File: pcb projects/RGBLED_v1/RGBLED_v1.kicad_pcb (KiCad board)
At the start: 2 copper layers, 63 x 43 mm, 25 parts, among them CN1 USB_B_Micro, CN2 Conn_01x03_Pin, J1 Conn_02x02_Odd_Even, SW1 SW_MEC_5E, U1 STM32F091RBTx, U3 LM1117T-3.3, Y1 32.768kHz

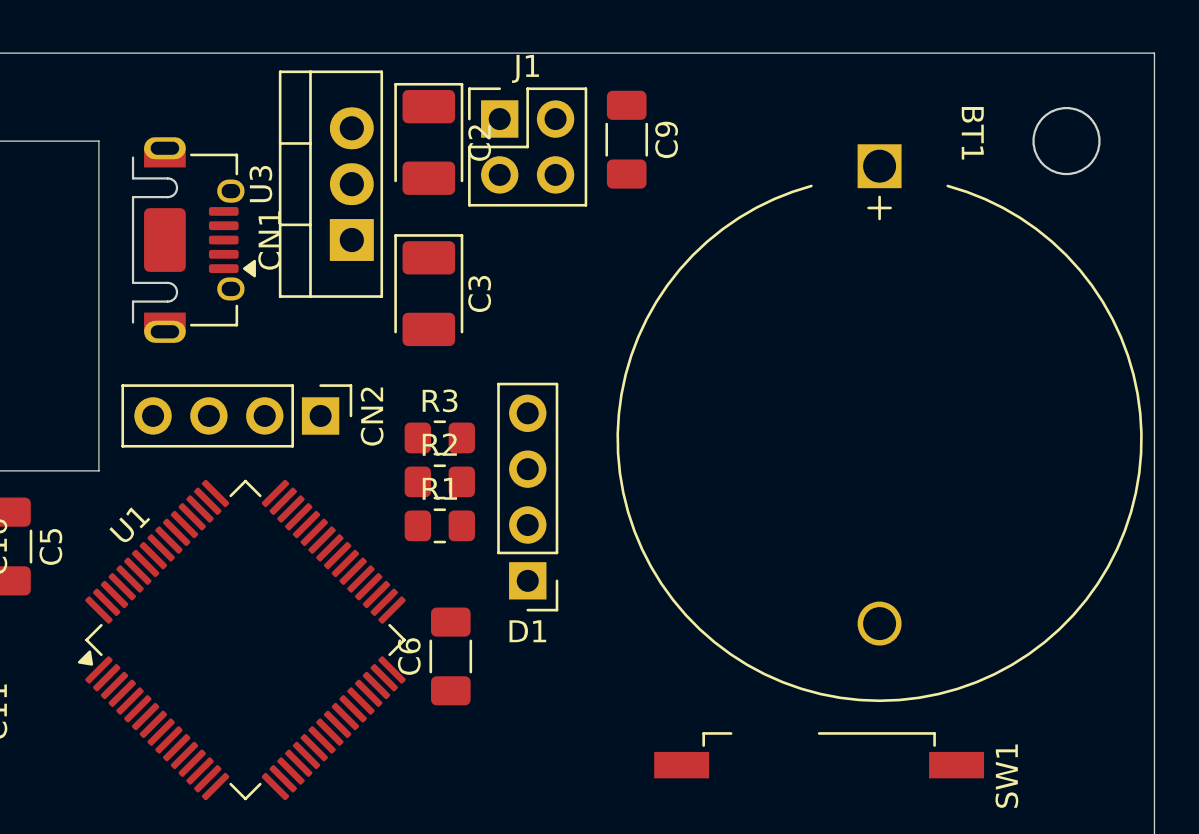
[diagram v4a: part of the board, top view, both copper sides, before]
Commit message: digital signal net class added
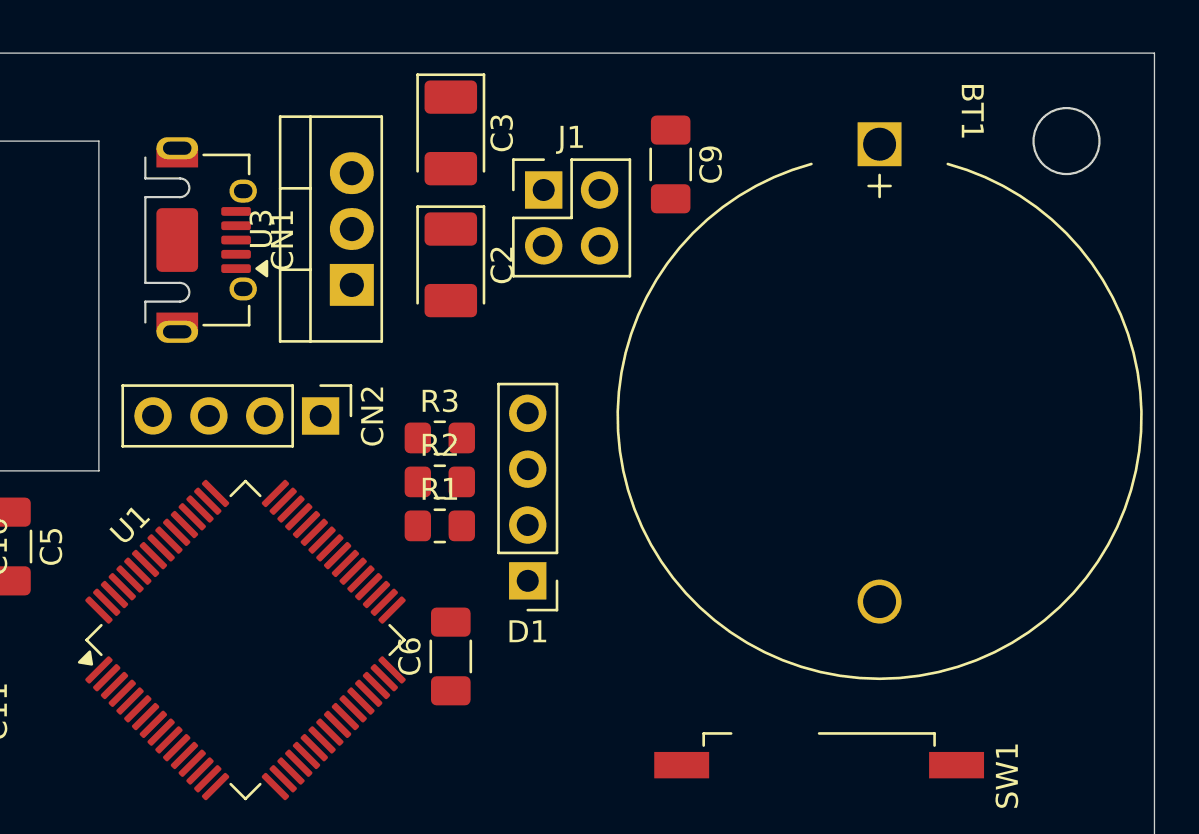
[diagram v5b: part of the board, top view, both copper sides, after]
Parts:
- moved C3 7.38 mm to (-0.50, -17.9)
- moved C2 5.65 mm to (-0.50, -11.9)
- moved J1 3.79 mm to (3.73, -15.3)
- moved C9 2.29 mm to (9.50, -16.4)
- moved U3 2.04 mm to (-5.00, -11.0)
- moved BT1 1.00 mm to (19.0, -17.4)
- moved CN1 0.56 mm to (-13.3, -13.0)
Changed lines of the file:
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@@
 	(footprint "Capacitor_Tantalum_SMD:CP_EIA-3528-21_Kemet-B_HandSolder"
 		(layer "F.Cu")
-		(at -1.5 -17.4375 -90)
+		(at -0.5 -11.8725 -90)
 		(descr "Tantalum Capacitor SMD Kemet-B (3528-21 Metric), IPC-7352 nominal, (Body size from: http://www.kemet.com/Lists/ProductCatalog/Attachments/253/KEM_TC101_STD.pdf), generated with kicad-footprint-generator")
 		(tags "capacitor tantalum")
@@
 	(footprint "Capacitor_SMD:C_1206_3216Metric_Pad1.33x1.80mm_HandSolder"
 		(layer "F.Cu")
-		(at 7.5 -17.5625 -90)
+		(at 9.5 -16.4375 -90)
 		(descr "Capacitor SMD 1206 (3216 Metric), square (rectangular) end terminal, IPC-7351 nominal with elongated pad for handsoldering. (Body size source: IPC-SM-782 page 76, https://www.pcb-3d.com/wordpress/wp-content/uploads/ipc-sm-782a_amendment_1_and_2.pdf), generated with kicad-footprint-generator")
 		(tags "capacitor handsolder")
@@
 	(footprint "Connector_USB:USB_Micro-AB_Molex_47590-0001"
 		(layer "F.Cu")
-		(at -13.85 -13 -90)
+		(at -13.29 -13 -90)
 		(descr "Micro USB AB receptacle, right-angle inverted (https://www.molex.com/pdm_docs/sd/475900001_sd.pdf)")
 		(tags "Micro AB USB SMD")
@@
 	(footprint "Battery:BatteryHolder_MYOUNG_BS-07-A1BJ001_CR2032"
 		(layer "F.Cu")
-		(at 19 -16.357454 -90)
+		(at 19 -17.357454 -90)
 		(descr "CR2032 battery holder https://www.lcsc.com/datasheet/lcsc_datasheet_2203021630_MYOUNG-BS-07-A1BJ001_C2979167.pdf")
 		(tags "CR2032 BR2032 BatteryHolder Battery")
@@
 	(footprint "Capacitor_Tantalum_SMD:CP_EIA-3528-21_Kemet-B_HandSolder"
 		(layer "F.Cu")
-		(at -1.5 -10.5625 -90)
+		(at -0.5 -17.8725 -90)
 		(descr "Tantalum Capacitor SMD Kemet-B (3528-21 Metric), IPC-7352 nominal, (Body size from: http://www.kemet.com/Lists/ProductCatalog/Attachments/253/KEM_TC101_STD.pdf), generated with kicad-footprint-generator")
 		(tags "capacitor tantalum")
@@
 	(footprint "Package_TO_SOT_THT:TO-220-3_Vertical"
 		(layer "F.Cu")
-		(at -5 -13 90)
+		(at -5 -10.96 90)
 		(descr "TO-220-3, Vertical, RM 2.54mm, see https://www.vishay.com/docs/66542/to-220-1.pdf, generated with kicad-footprint-generator TO_SOT_THT_generate.py")
 		(tags "TO-220-3 Vertical RM 2.54mm")
@@
 	(footprint "Connector_PinHeader_2.54mm:PinHeader_2x02_P2.54mm_Vertical"
 		(layer "F.Cu")
-		(at 1.725 -18.5)
+		(at 3.725 -15.275)
 		(descr "Through hole straight pin header, 2x02, 2.54mm pitch, double rows")
 		(tags "Through hole pin header THT 2x02 2.54mm double row")

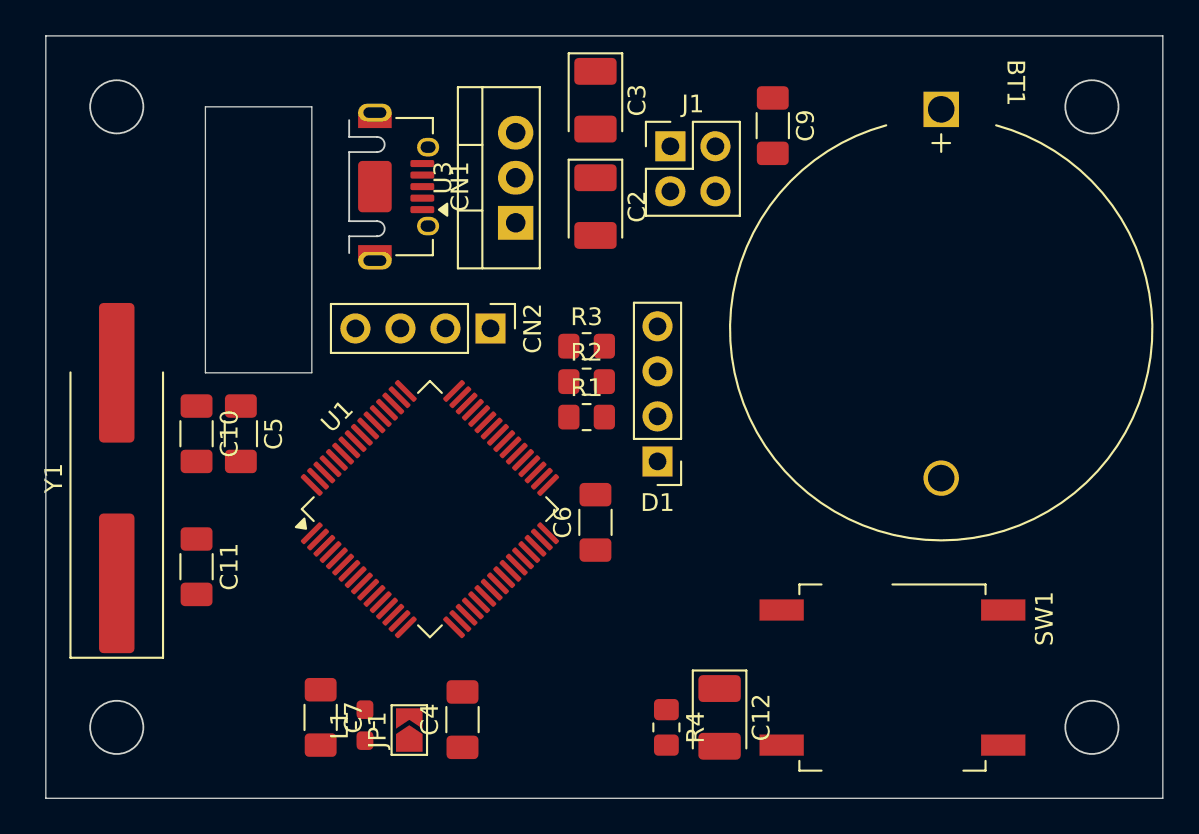
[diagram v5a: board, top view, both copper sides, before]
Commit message: wired small traces, gnd polygon overwiev, no 3v3 trace
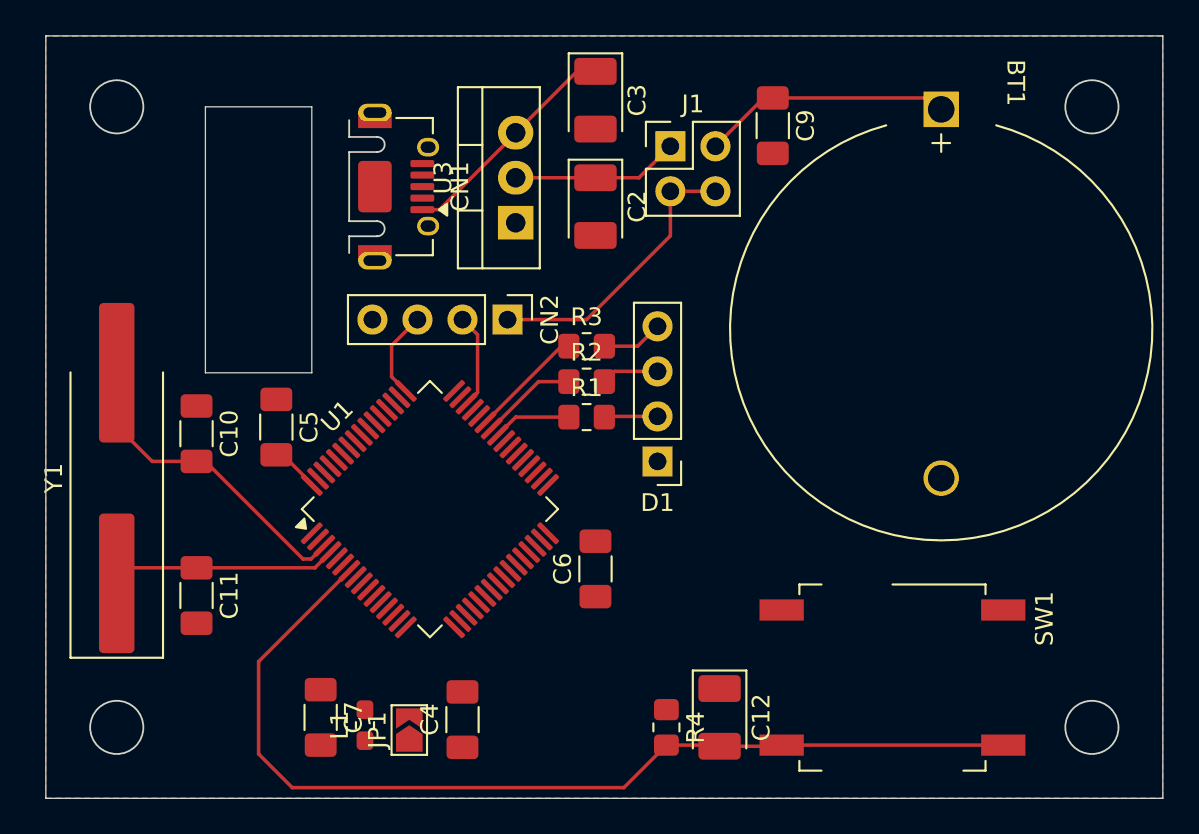
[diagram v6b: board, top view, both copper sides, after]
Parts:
- moved C6 2.62 mm to (-0.50, 8.56)
- moved C5 2.03 mm to (-18.5, 0.56)
- moved C11 1.62 mm to (-23.0, 10.1)
- moved CN2 1.08 mm to (-5.46, -5.50)
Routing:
- net /nRST: track 0.00 -> 56.3 mm
- net +3.3V: track 0.00 -> 18.9 mm
- net Net-(U1-PC14): track 0.00 -> 18.1 mm
- net Net-(BT1-+): track 0.00 -> 14.1 mm
- net +5V: track 0.00 -> 13.0 mm
- net Net-(U1-PC15): track 0.00 -> 12.8 mm
- net Net-(J1-Pin_1): track 0.00 -> 9.46 mm
- net Net-(U1-PA10): track 0.00 -> 6.49 mm
- net Net-(U1-PA9): track 0.00 -> 5.45 mm
- net /TCK: track 0.00 -> 5.34 mm
- net /TMS: track 0.00 -> 4.96 mm
- net Net-(U1-PA8): track 0.00 -> 4.41 mm
- net Net-(D1-BK): track 0.00 -> 3.46 mm
- net Net-(D1-GK): track 0.00 -> 3.24 mm
- net Net-(D1-RK): track 0.00 -> 3.02 mm
- added copper zone on F.Cu, net GND

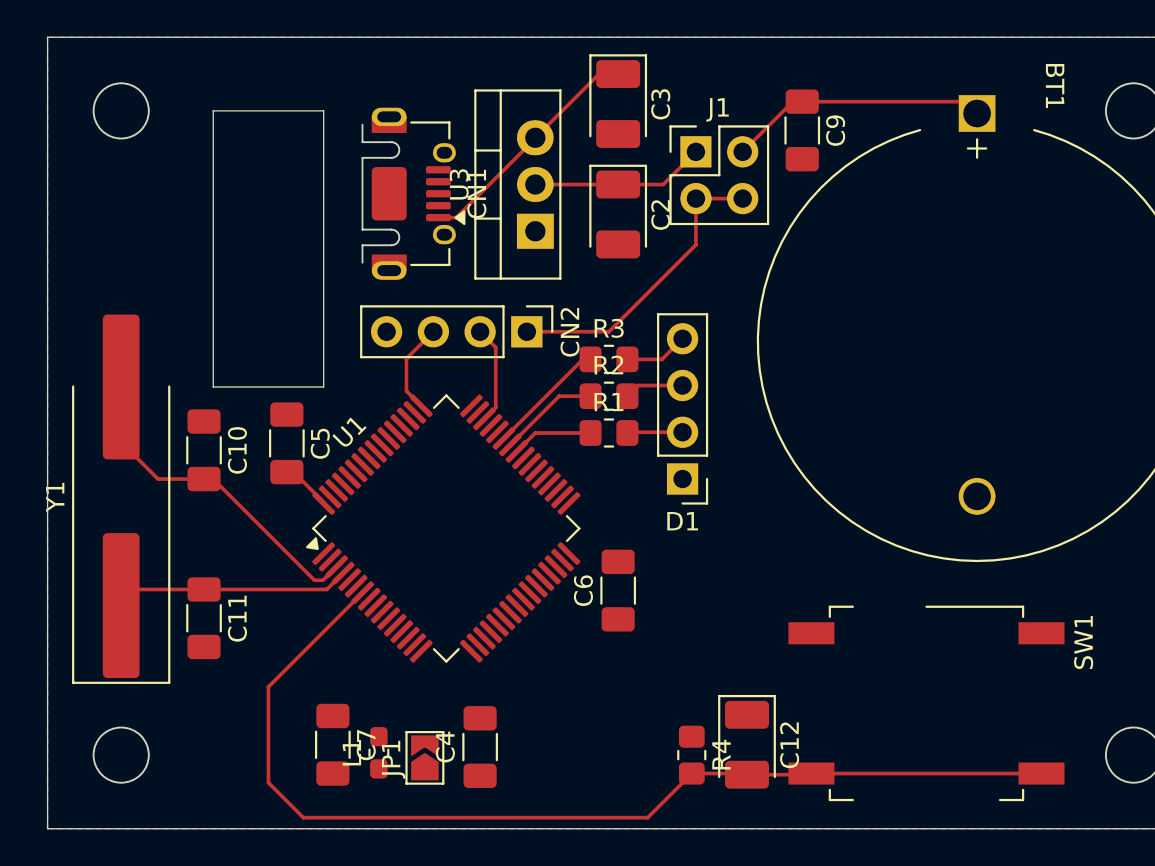
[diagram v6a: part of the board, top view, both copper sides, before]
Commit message: traces done, GND plygon left
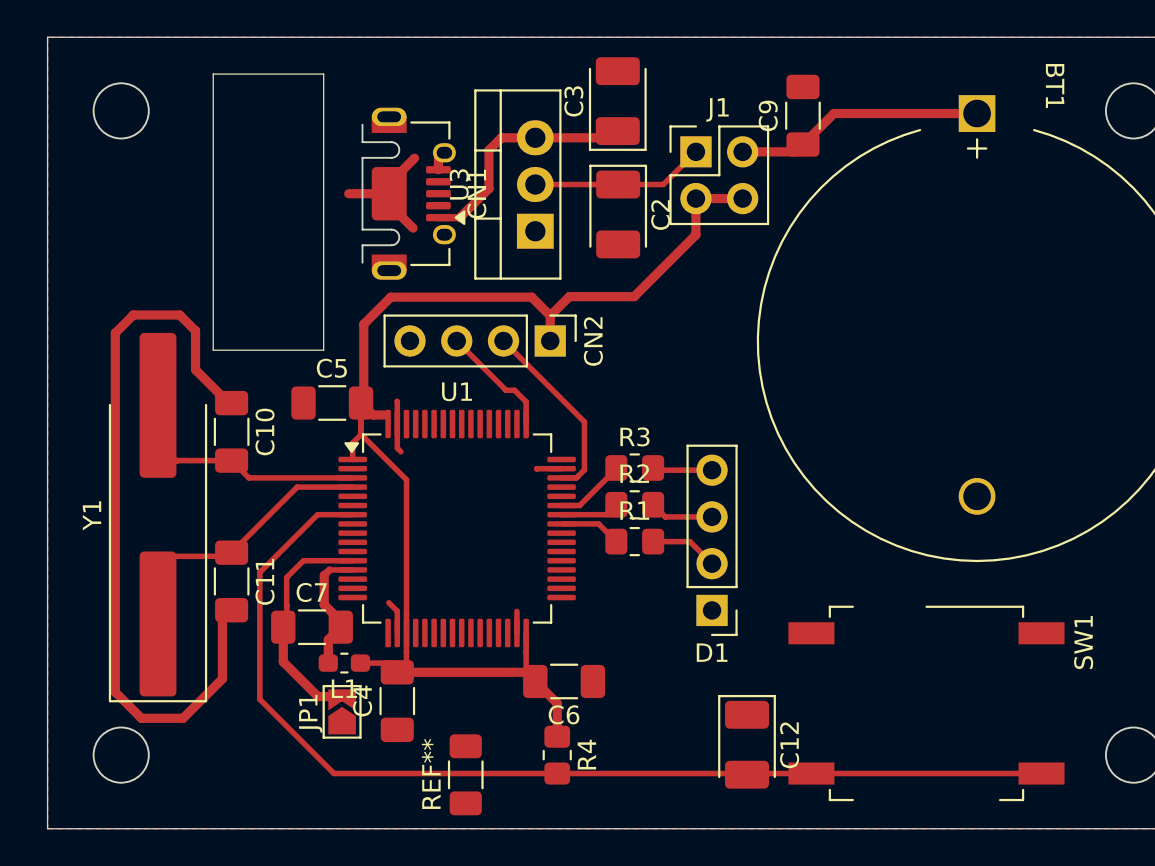
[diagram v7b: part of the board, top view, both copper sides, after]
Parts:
- added REF**: R_1206_3216Metric_Pad1.30x1.75mm_HandSolder, Resistor_SMD:R_1206_3216Metric_Pad1.30x1.75mm_HandSolder, F.Cu at (-8.78, 18.6)
- moved D1 7.32 mm to (4.60, 9.64)
- moved R4 7.31 mm to (-3.81, 17.5)
- moved C7 6.49 mm to (-17.1, 10.6), turned to 0 degrees
- moved R1 6.06 mm to (0.40, 5.90)
- moved R2 6.06 mm to (0.40, 3.90)
- moved R3 6.06 mm to (0.40, 1.90)
- moved C6 5.75 mm to (-3.44, 13.5), turned to 180 degrees
- moved L1 5.22 mm to (-15.4, 12.5), turned to 180 degrees
- moved C4 5.15 mm to (-12.5, 14.6)
- moved JP1 5.15 mm to (-15.5, 15.2)
- moved C5 3.30 mm to (-16.0, -1.63), turned to 0 degrees
- moved C11 2.50 mm to (-21.5, 8.06)
- moved Y1 2.24 mm to (-25.5, 4.44)
- moved C10 1.80 mm to (-21.5, -0.06)
- moved CN2 1.36 mm to (-4.19, -5.00)
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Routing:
- net GND: track 0.00 -> 56.1 mm
- net +3.3V: track 18.9 -> 68.0 mm
- net GNDA: track 0.00 -> 12.4 mm
- net AVDD: track 0.00 -> 7.09 mm
- net /TCK: track 5.34 -> 10.3 mm
- net Net-(U1-PC15): track 12.8 -> 16.6 mm
- net Net-(U1-PA9): track 5.45 -> 3.20 mm
- net Net-(U1-PA10): track 6.49 -> 4.26 mm
- net Net-(U1-PC14): track 18.1 -> 16.4 mm
- net /TMS: track 4.96 -> 6.35 mm
- net /nRST: track 56.3 -> 57.4 mm
- net Net-(U1-PA8): track 4.41 -> 3.28 mm
- net Net-(D1-RK): track 3.02 -> 3.70 mm
- net Net-(BT1-+): track 14.1 -> 13.6 mm
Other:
- outline, holes or cut-outs redrawn
